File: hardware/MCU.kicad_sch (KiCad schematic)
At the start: 9 parts, among them U1 STM32G0C1KCTxN

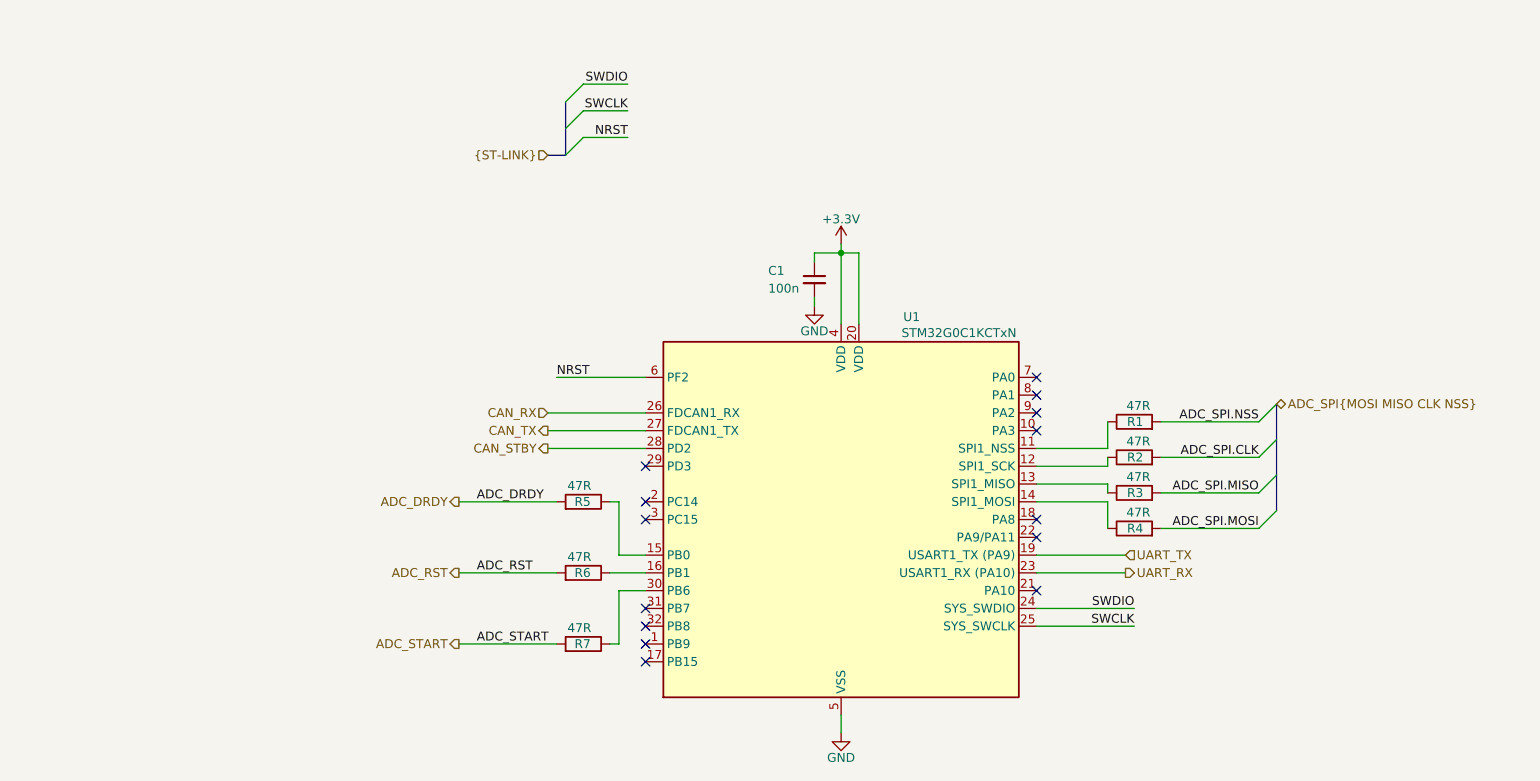
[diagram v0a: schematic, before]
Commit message: Finished routing on PCB
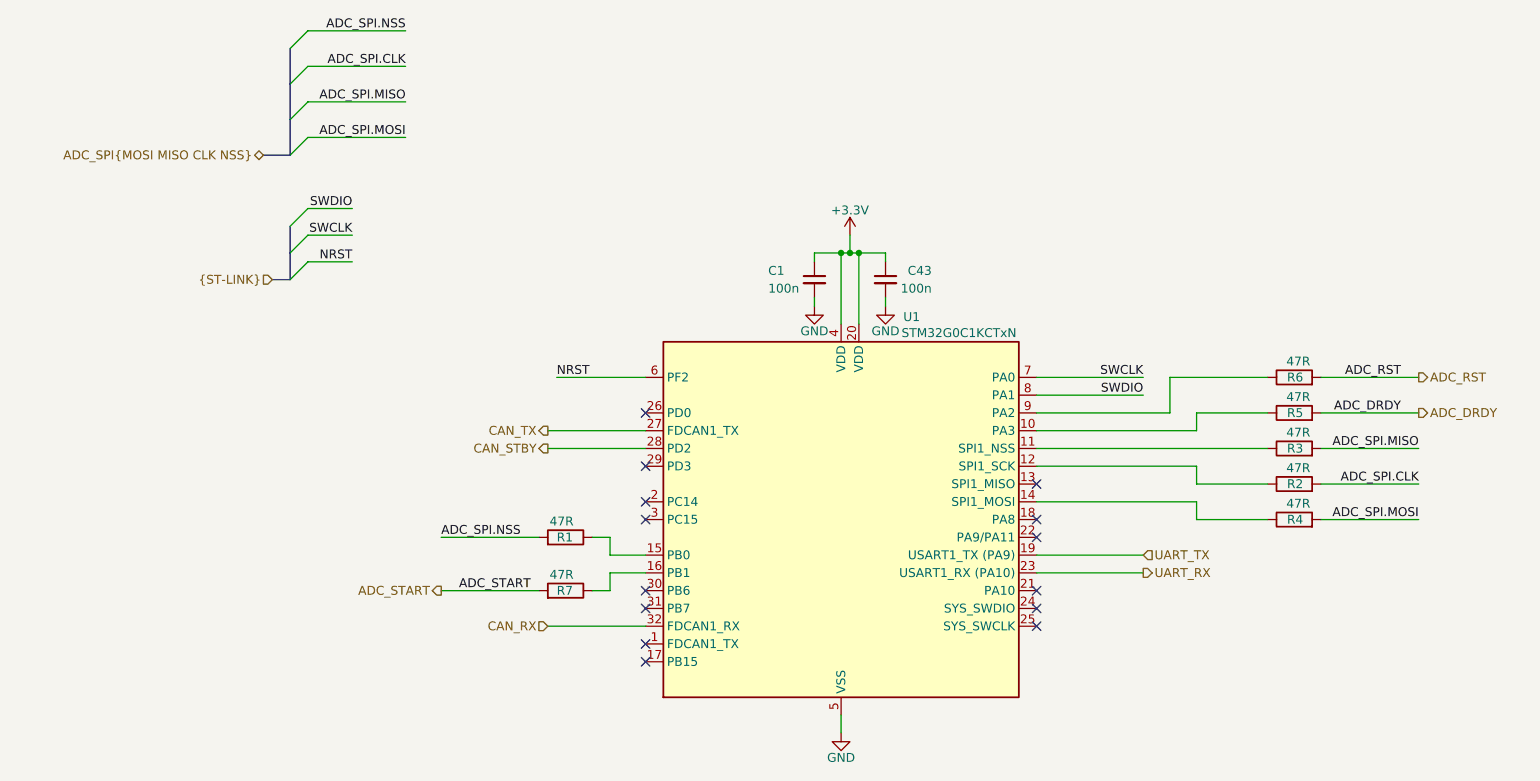
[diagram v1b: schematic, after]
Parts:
- added C43: 100n, Capacitor_SMD:C_0603_1608Metric_Pad1.08x0.95mm_HandSolder, symbol Device:C_Small
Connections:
- net +3.3V: now also C43.1
- net CAN_RX: now also U1.32 (PB8); no longer U1.26 (PD0)
- net GND: now also C43.2
- net SWCLK: now also U1.7 (PA0); no longer U1.25 (PA14)
- net SWDIO: now also U1.8 (PA1); no longer U1.24 (PA13)
- net at R7.1: now also U1.16 (PB1); no longer U1.30 (PB6)
- net at R5.1: now also U1.10 (PA3); no longer U1.15 (PB0)
- net at R6.1: now also U1.9 (PA2); no longer U1.16 (PB1)
- net at R1.1: now also U1.15 (PB0); no longer U1.11 (PA4)
- net at R3.1: now also U1.11 (PA4); no longer U1.13 (PA6)
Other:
- moved on the sheet: R1, R2, R3, R4, R5, R6, R7

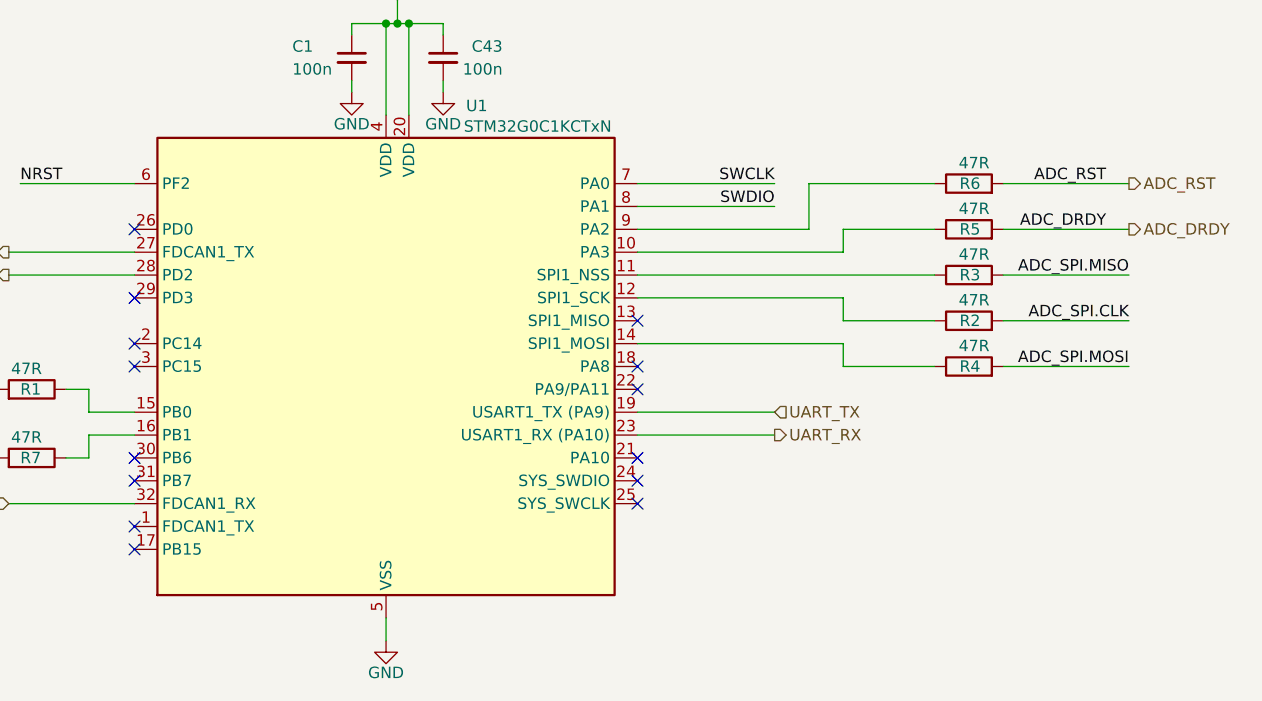
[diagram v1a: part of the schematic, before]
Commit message: Fixed pinout errors & changed branch name
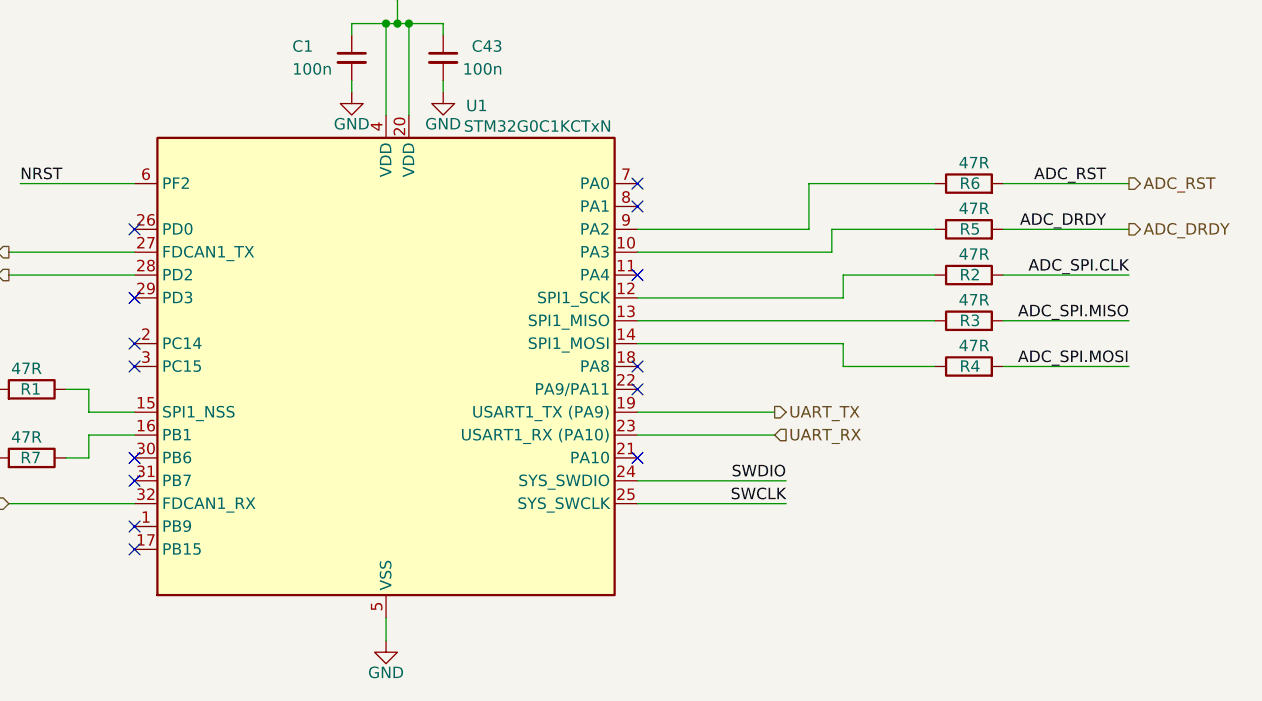
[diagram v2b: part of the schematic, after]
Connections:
- net SWCLK: now also U1.25 (PA14); no longer U1.7 (PA0)
- net SWDIO: now also U1.24 (PA13); no longer U1.8 (PA1)
- net at R3.1: now also U1.13 (PA6); no longer U1.11 (PA4)
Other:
- moved on the sheet: R2, R3
